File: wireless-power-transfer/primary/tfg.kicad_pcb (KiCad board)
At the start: 2 copper layers, 160 x 100 mm, 30 parts, among them J1 CONN_01X06, J2 Screw_Terminal_1x02, J3 BARREL_JACK, Q1 IRLB8721PBF, Q2 IRLB8721PBF, Q3 IRLB8721PBF, Q4 IRLB8721PBF, U1 PIC18F45K20-I/PT, U2 IR2110, U3 IR2110, U4 R-78E15, U5 R-78E3.3, U6 XBEE_Wi-Fi

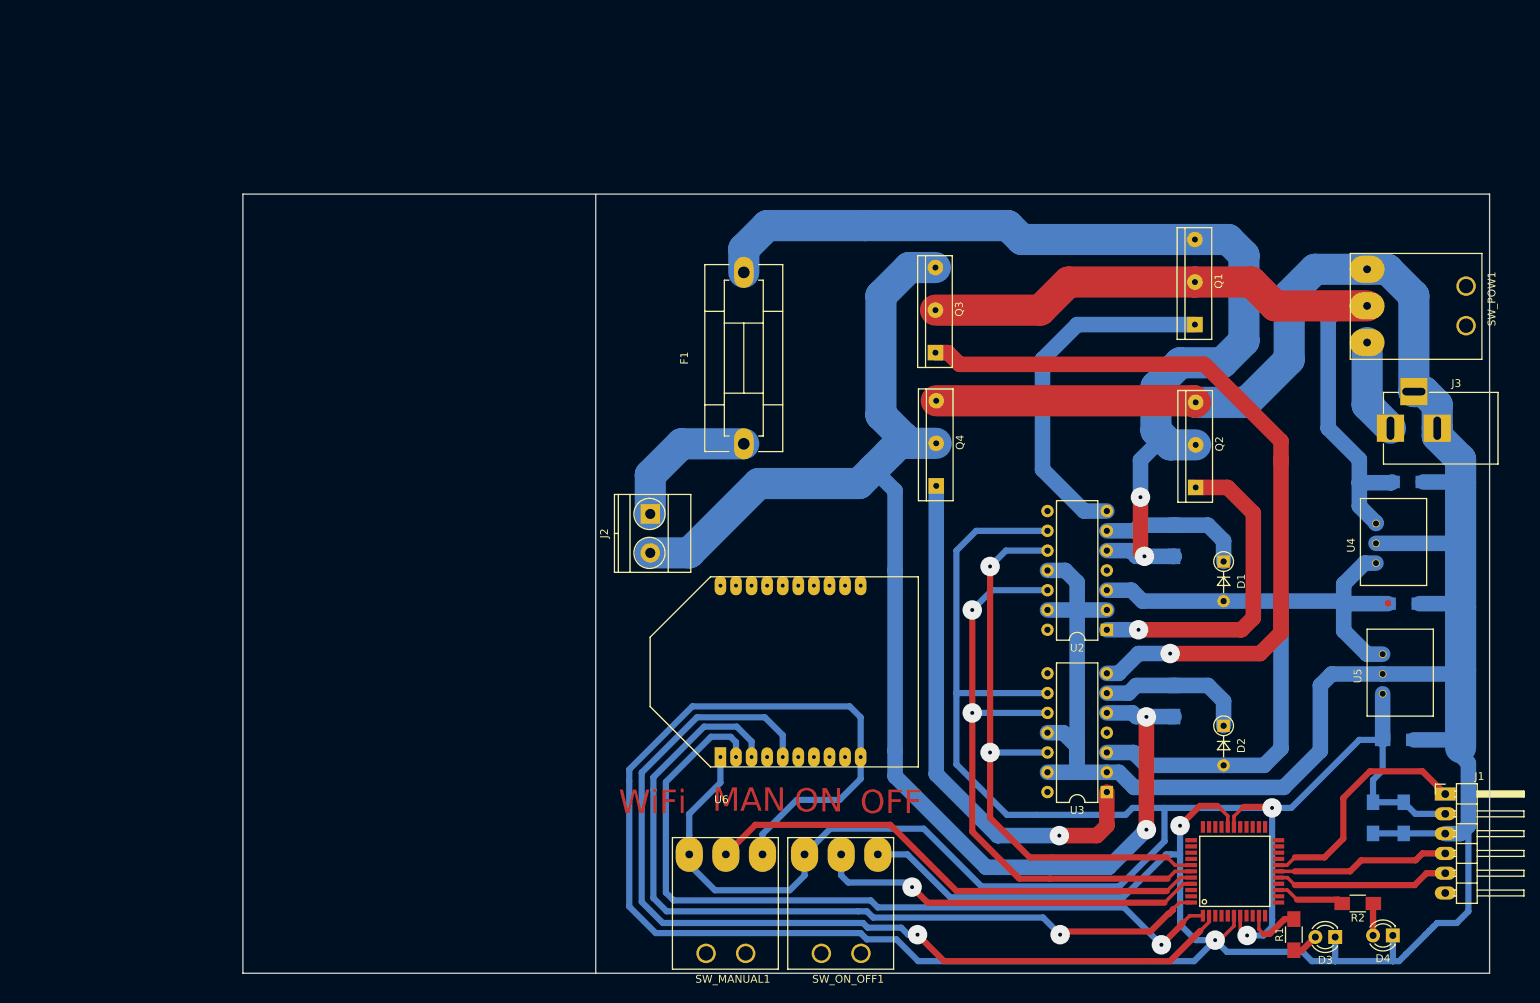
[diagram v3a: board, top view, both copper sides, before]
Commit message: Added pcb with tank and filter of the primary, some logos and other minor changes.
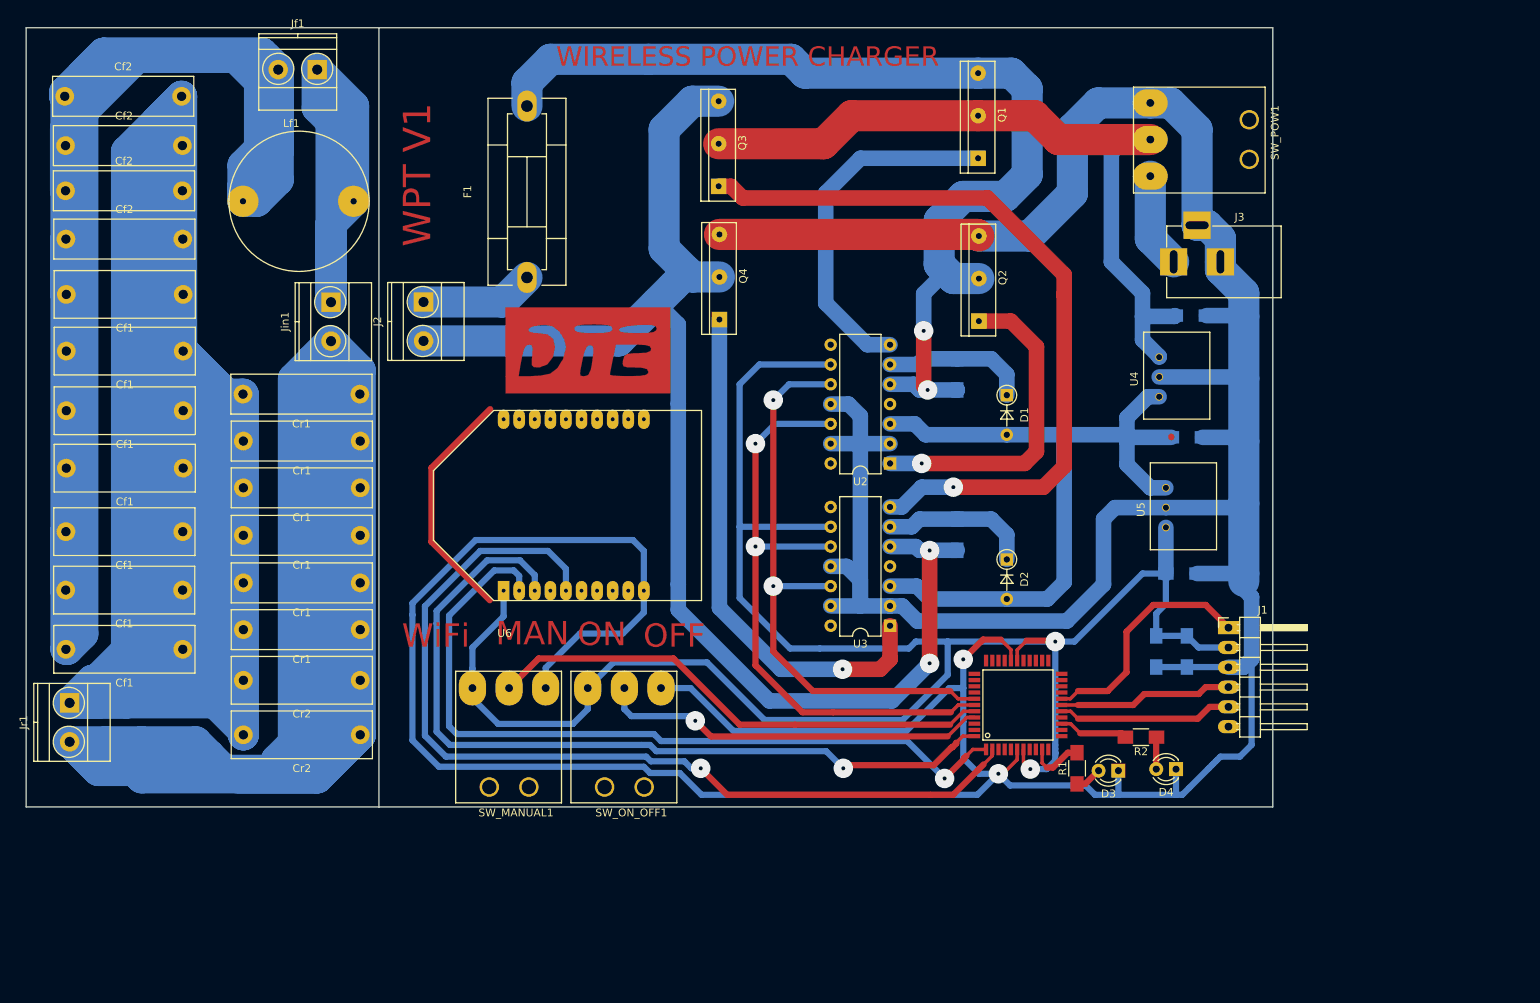
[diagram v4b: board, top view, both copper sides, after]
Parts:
- added Cf1: 10nF, Capacitors_THT:C_Rect_L18.0mm_W6.0mm_P15.00mm_FKS3_FKP3, F.Cu at (78.0, 59.8)
- added Cf1: C, Capacitors_THT:C_Rect_L18.0mm_W6.0mm_P15.00mm_FKS3_FKP3, F.Cu at (78.0, 67.1)
- added Cf1: C, Capacitors_THT:C_Rect_L18.0mm_W6.0mm_P15.00mm_FKS3_FKP3, F.Cu at (78.0, 74.8)
- added Cf1: C, Capacitors_THT:C_Rect_L18.0mm_W6.0mm_P15.00mm_FKS3_FKP3, F.Cu at (78.0, 82.1)
- added Cf1: C, Capacitors_THT:C_Rect_L18.0mm_W6.0mm_P15.00mm_FKS3_FKP3, F.Cu at (78.0, 90.3)
- added Cf1: C, Capacitors_THT:C_Rect_L18.0mm_W6.0mm_P15.00mm_FKS3_FKP3, F.Cu at (78.0, 97.8)
- added Cf1: C, Capacitors_THT:C_Rect_L18.0mm_W6.0mm_P15.00mm_FKS3_FKP3, F.Cu at (78.0, 105.4)
- added Cf2: 2.2nF, Capacitors_THT:C_Rect_L18.0mm_W5.0mm_P15.00mm_FKS3_FKP3, F.Cu at (62.9, 34.4)
- added Cf2: C, Capacitors_THT:C_Rect_L18.0mm_W5.0mm_P15.00mm_FKS3_FKP3, F.Cu at (63.0, 40.7)
- added Cf2: C, Capacitors_THT:C_Rect_L18.0mm_W5.0mm_P15.00mm_FKS3_FKP3, F.Cu at (63.0, 46.5)
- added Cf2: C, Capacitors_THT:C_Rect_L18.0mm_W5.0mm_P15.00mm_FKS3_FKP3, F.Cu at (63.0, 52.7)
- added Cr1: 100nF, Capacitors_THT:C_Rect_L18.0mm_W5.0mm_P15.00mm_FKS3_FKP3, F.Cu at (100.7, 72.6)
- added Cr1: 100nF, Capacitors_THT:C_Rect_L18.0mm_W5.0mm_P15.00mm_FKS3_FKP3, F.Cu at (100.8, 78.7)
- added Cr1: 100nF, Capacitors_THT:C_Rect_L18.0mm_W5.0mm_P15.00mm_FKS3_FKP3, F.Cu at (100.8, 84.7)
- added Cr1: 100nF, Capacitors_THT:C_Rect_L18.0mm_W5.0mm_P15.00mm_FKS3_FKP3, F.Cu at (100.8, 90.8)
- added Cr1: 100nF, Capacitors_THT:C_Rect_L18.0mm_W5.0mm_P15.00mm_FKS3_FKP3, F.Cu at (100.8, 96.8)
- added Cr1: 100nF, Capacitors_THT:C_Rect_L18.0mm_W5.0mm_P15.00mm_FKS3_FKP3, F.Cu at (100.8, 102.8)
- added Cr2: 10nF, Capacitors_THT:C_Rect_L18.0mm_W6.0mm_P15.00mm_FKS3_FKP3, F.Cu at (100.8, 116.3)
- added Cr2: 10nF, Capacitors_THT:C_Rect_L18.0mm_W6.0mm_P15.00mm_FKS3_FKP3, F.Cu at (100.8, 109.3)
- added G***: LOGO, componentesGIT:DTE, F.Cu at (130.0, 67.0)
- added Jf1: Screw_Terminal_1x02, Connectors_Terminal_Blocks:TerminalBlock_Pheonix_MKDS1.5-2pol, F.Cu at (95.2, 31.0)
- added Jin1: Screw_Terminal_1x02, Connectors_Terminal_Blocks:TerminalBlock_Pheonix_MKDS1.5-2pol, F.Cu at (97.0, 60.8)
- added Jr1: Screw_Terminal_1x02, Connectors_Terminal_Blocks:TerminalBlock_Pheonix_MKDS1.5-2pol, F.Cu at (63.5, 112.2)
- added Lf1: 47uH, componentesGIT:MuRata 1500 47u, F.Cu at (99.9, 47.9)
- moved J2 39.8 mm to (108.9, 60.8)
- moved C5 35.1 mm to (207.4, 62.5)
- moved D3 35.1 mm to (198.1, 121.0)
- moved D4 35.1 mm to (205.5, 120.8)
- moved Q1 35.1 mm to (180.1, 42.4)
- moved R2 35.1 mm to (201.0, 116.7)
- moved SW_ON_OFF1 35.1 mm to (130.0, 110.3)
- moved U2 35.1 mm to (168.8, 81.5)
- moved U3 35.1 mm to (168.8, 102.3)
- moved U6 35.1 mm to (119.2, 97.8)
- moved F1 35.1 mm to (122.2, 57.6)
- moved SW_MANUAL1 35.1 mm to (115.2, 110.3)
- moved C6 35.1 mm to (206.9, 78.2)
- moved Q4 35.1 mm to (146.9, 63.0)
- moved U1 35.1 mm to (189.1, 118.2)
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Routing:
- net Net-(Cf1-Pad1): track 0.00 -> 479.9 mm
- net Net-(Cr1-Pad1): track 0.00 -> 370.0 mm
- net Net-(Cf1-Pad2): track 0.00 -> 347.0 mm
- net Net-(Jf1-Pad1): track 0.00 -> 63.6 mm
- net (no net): track 0.09 -> 30.8 mm
- net Net-(F1-Pad1): track 18.7 -> 14.6 mm
- net Net-(Cboot2-Pad2): track 174.2 -> 173.1 mm
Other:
- board text added: "WIRELESS POWER CHARGER"
- board text added: "WPT V1"

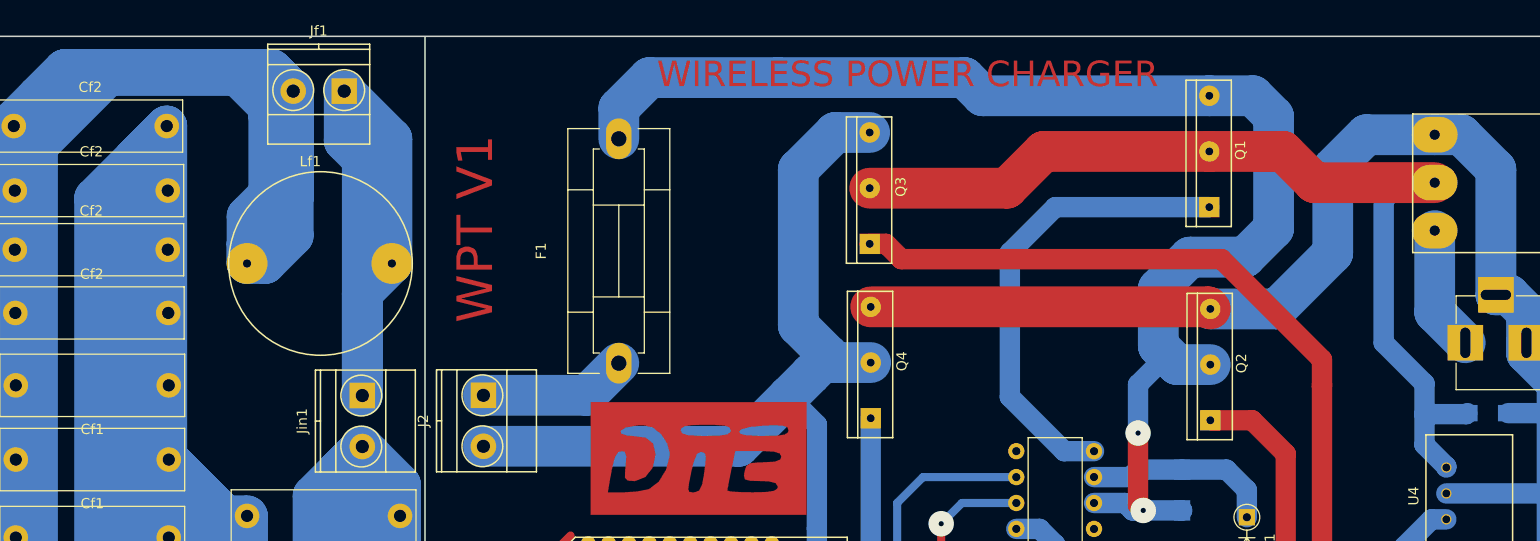
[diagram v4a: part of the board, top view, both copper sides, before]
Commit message: Modified secondary PCB for better fitting in the car.
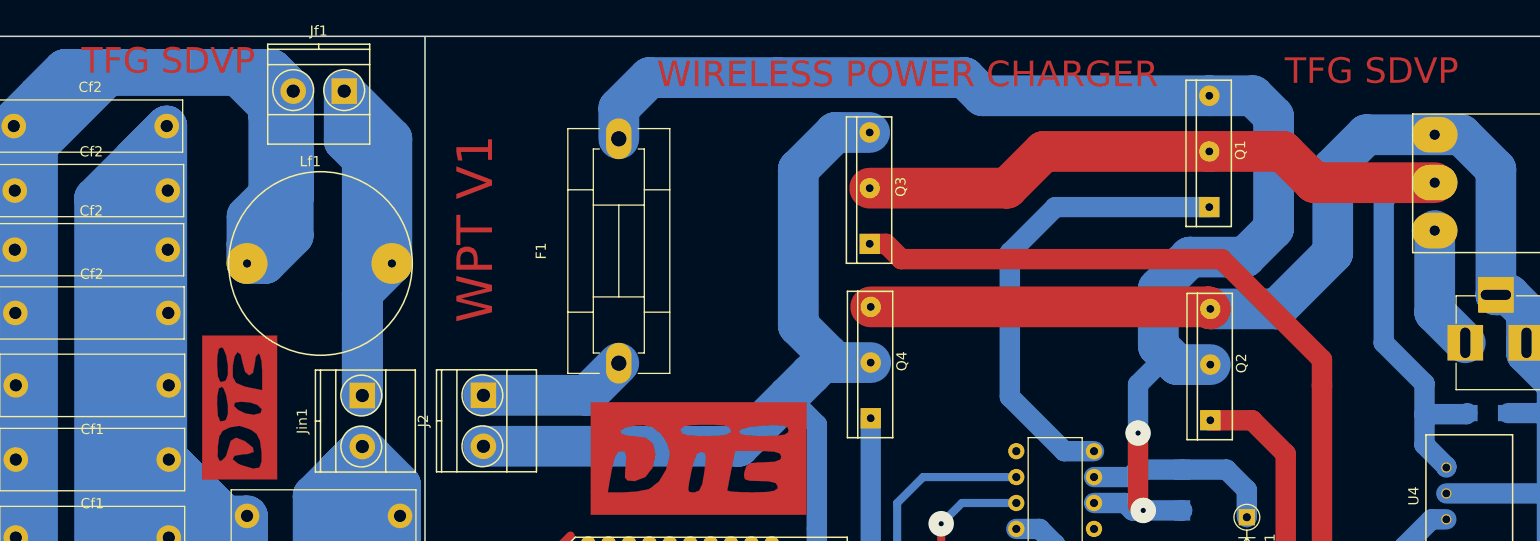
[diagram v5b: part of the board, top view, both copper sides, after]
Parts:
- added G***: LOGO, componentesGIT:DTE_Micro, F.Cu at (85.0, 62.0)
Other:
- board text added: "TFG SDVP"
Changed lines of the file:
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@@
     (area 56.3 23.8 223.280001 127.727)
     (thickness 1.6)
-    (drawings 19)
+    (drawings 21)
     (tracks 579)
     (zones 0)
-    (modules 54)
+    (modules 55)
     (nets 77)
   )
@@
   )
   (setup
-    (last_trace_width 4)
+    (last_trace_width 0.8)
     (user_trace_width 0.45)
     (user_trace_width 0.8)
@@
       (xy -8.897967 3.313043) (xy -10.583333 3.313043) (xy -10.583333 -5.521739) (xy 10.583333 -5.521739)
       (xy 10.583333 5.521739)) (layer F.Cu) (width 0.01))
+  )
+  (module componentesGIT:DTE_Micro (layer F.Cu)
+    (at 85 62 90)
+    (fp_text reference G*** (at 3 5 90) (layer F.SilkS) hide
+      (effects (font (thickness 0.3)))
+    )
+    (fp_text value LOGO (at -1 -5 90) (layer F.SilkS) hide
+      (effects (font (thickness 0.3)))
+    )
+    (fp_poly (pts (xy 7.055556 3.681159) (xy -7.055555 3.681159) (xy -7.055555 2.208696) (xy 1.707829 2.208696)
+      (xy 3.499748 2.208696) (xy 4.515097 2.143458) (xy 5.164544 1.976405) (xy 5.291667 1.84058)
+      (xy 4.985114 1.582113) (xy 4.2465 1.472492) (xy 4.233333 1.472464) (xy 3.401368 1.307936)
+      (xy 3.154326 0.935662) (xy 3.478527 0.537606) (xy 4.321528 0.29941) (xy 5.202345 0.095434)
+      (xy 5.42692 -0.203464) (xy 5.018786 -0.495004) (xy 4.09865 -0.669316) (xy 3.023344 -0.678138)
+      (xy 2.419037 -0.357361) (xy 2.073198 0.459307) (xy 1.949414 1.012319) (xy 1.707829 2.208696)
+      (xy -7.055555 2.208696) (xy -7.055555 1.328457) (xy -5.985372 1.328457) (xy -5.887546 1.933839)
+      (xy -5.271327 2.153272) (xy -4.332934 2.136836) (xy -3.229709 1.987754) (xy -2.574031 1.645596)
+      (xy -2.369213 1.358764) (xy -0.705555 1.358764) (xy -0.541721 2.051698) (xy -0.166878 2.171356)
+      (xy 0.243983 1.760742) (xy 0.483497 1.06654) (xy 0.57094 0.147434) (xy 0.474176 -0.460959)
+      (xy 0.473745 -0.46169) (xy 0.151341 -0.554444) (xy -0.240374 -0.14451) (xy -0.569845 0.56503)
+      (xy -0.705555 1.358764) (xy -2.369213 1.358764) (xy -2.139721 1.037378) (xy -1.798295 -0.020864)
+      (xy -1.958475 -0.98726) (xy -2.286304 -1.661404) (xy -2.667334 -1.894563) (xy -1.366925 -1.894563)
+      (xy -1.282289 -1.47517) (xy -1.159326 -1.332437) (xy -0.623942 -1.156524) (xy 0.252223 -1.162251)
+      (xy 1.177504 -1.311567) (xy 1.860235 -1.566425) (xy 2.030452 -1.748551) (xy 1.957835 -1.894563)
+      (xy 2.51363 -1.894563) (xy 2.598267 -1.47517) (xy 2.72123 -1.332437) (xy 3.256614 -1.156524)
+      (xy 4.132779 -1.162251) (xy 5.058059 -1.311567) (xy 5.740791 -1.566425) (xy 5.911008 -1.748551)
+      (xy 5.765432 -2.041259) (xy 5.043581 -2.185147) (xy 4.262732 -2.208696) (xy 3.058004 -2.133132)
+      (xy 2.51363 -1.894563) (xy 1.957835 -1.894563) (xy 1.884876 -2.041259) (xy 1.163026 -2.185147)
+      (xy 0.382176 -2.208696) (xy -0.822552 -2.133132) (xy -1.366925 -1.894563) (xy -2.667334 -1.894563)
+      (xy -2.832943 -1.995902) (xy -3.835668 -2.139707) (xy -4.81399 -2.154547) (xy -5.210979 -1.983469)
+      (xy -5.212598 -1.771591) (xy -4.781138 -1.353016) (xy -4.205701 -1.165206) (xy -3.255826 -0.880097)
+      (xy -2.956663 -0.353027) (xy -3.274237 0.480216) (xy -3.30708 0.533272) (xy -3.925002 1.300933)
+      (xy -4.356336 1.375278) (xy -4.569145 0.760432) (xy -4.586111 0.368116) (xy -4.724004 -0.496511)
+      (xy -5.06238 -0.684596) (xy -5.48829 -0.179191) (xy -5.653176 0.208022) (xy -5.985372 1.328457)
+      (xy -7.055555 1.328457) (xy -7.055555 -3.681159) (xy 7.055556 -3.681159) (xy 7.055556 3.681159)) (layer F.Cu) (width 0.01))
+  )
+  (gr_text "TFG SDVP" (at 78 28) (layer F.Cu)
+    (effects (font (size 2.5 2.5) (thickness 0.5)))
+  )
+  (gr_text "TFG SDVP" (at 196 29) (layer F.Cu)
+    (effects (font (size 2.5 2.5) (thickness 0.5)))
   )
   (gr_text "WIRELESS POWER CHARGER" (at 150.5 29.325) (layer F.Cu)
@@
   (segment (start 70.775 105.5) (end 70.9 105.375) (width 4) (layer B.Cu) (net 73))
   (segment (start 70.9 105.375) (end 78 105.375) (width 4) (layer B.Cu) (net 73))
-  (segment (start 63 52.725) (end 63 59.775) (width 4) (layer B.Cu) (net 74) (status C00000))
-  (segment (start 63 59.775) (end 63.05 59.825) (width 4) (layer B.Cu) (net 74) (status C00000))
-  (segment (start 62.95 40.725) (end 62.95 46.525) (width 4) (layer B.Cu) (net 74) (status C00000))
-  (segment (start 62.975 97.775) (end 62.975 90.3) (width 4) (layer B.Cu) (net 74) (status C00000))
-  (segment (start 62.975 90.3) (end 63 90.275) (width 4) (layer B.Cu) (net 74) (status C00000))
+  (segment (start 63 52.725) (end 63 59.775) (width 4) (layer B.Cu) (net 74))
+  (segment (start 63 59.775) (end 63.05 59.825) (width 4) (layer B.Cu) (net 74))
+  (segment (start 62.95 40.725) (end 62.95 46.525) (width 4) (layer B.Cu) (net 74))
+  (segment (start 62.975 97.775) (end 62.975 90.3) (width 4) (layer B.Cu) (net 74))
+  (segment (start 62.975 90.3) (end 63 90.275) (width 4) (layer B.Cu) (net 74))
   (segment (start 85.725 47.875) (end 85.725 43.25) (width 4) (layer B.Cu) (net 74))
   (segment (start 87.85 33.375) (end 90.25 30.975) (width 4) (layer B.Cu) (net 74))

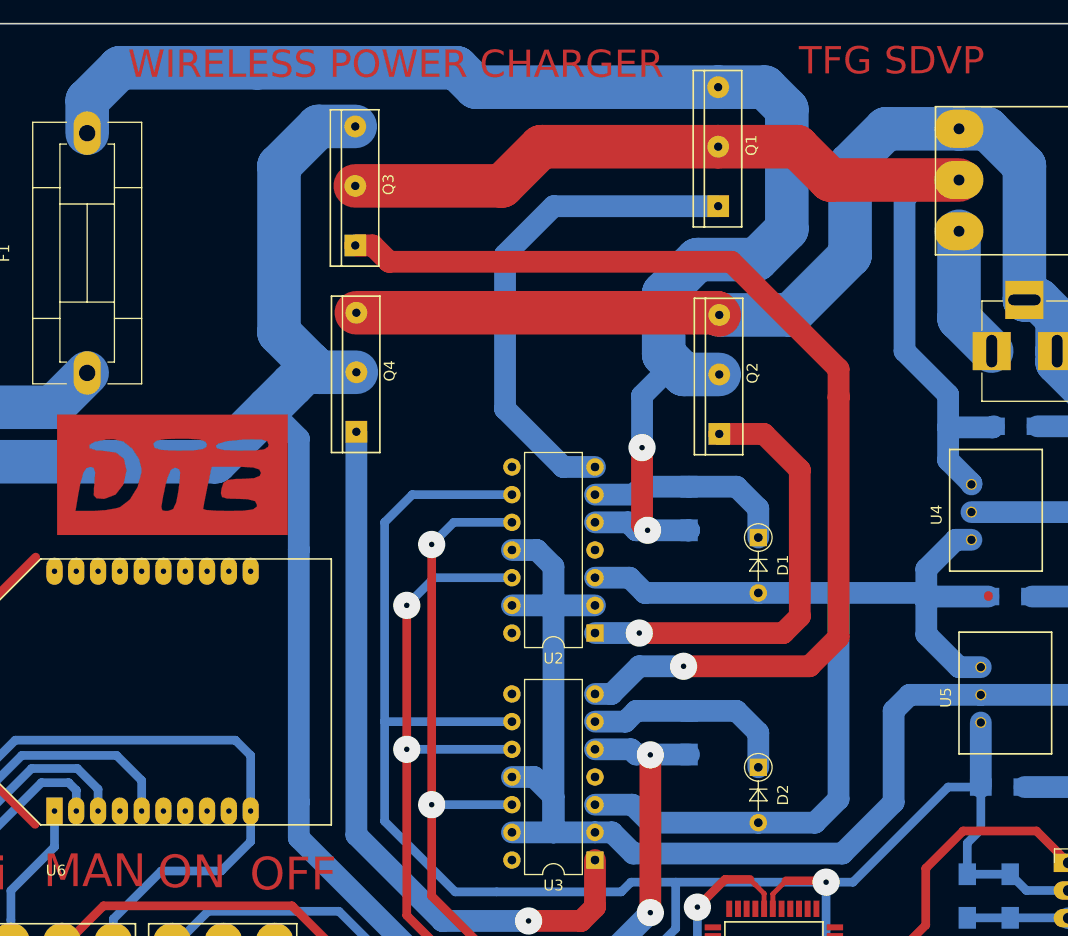
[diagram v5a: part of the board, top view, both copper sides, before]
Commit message: modified pad sizes and secondary PCB layout.
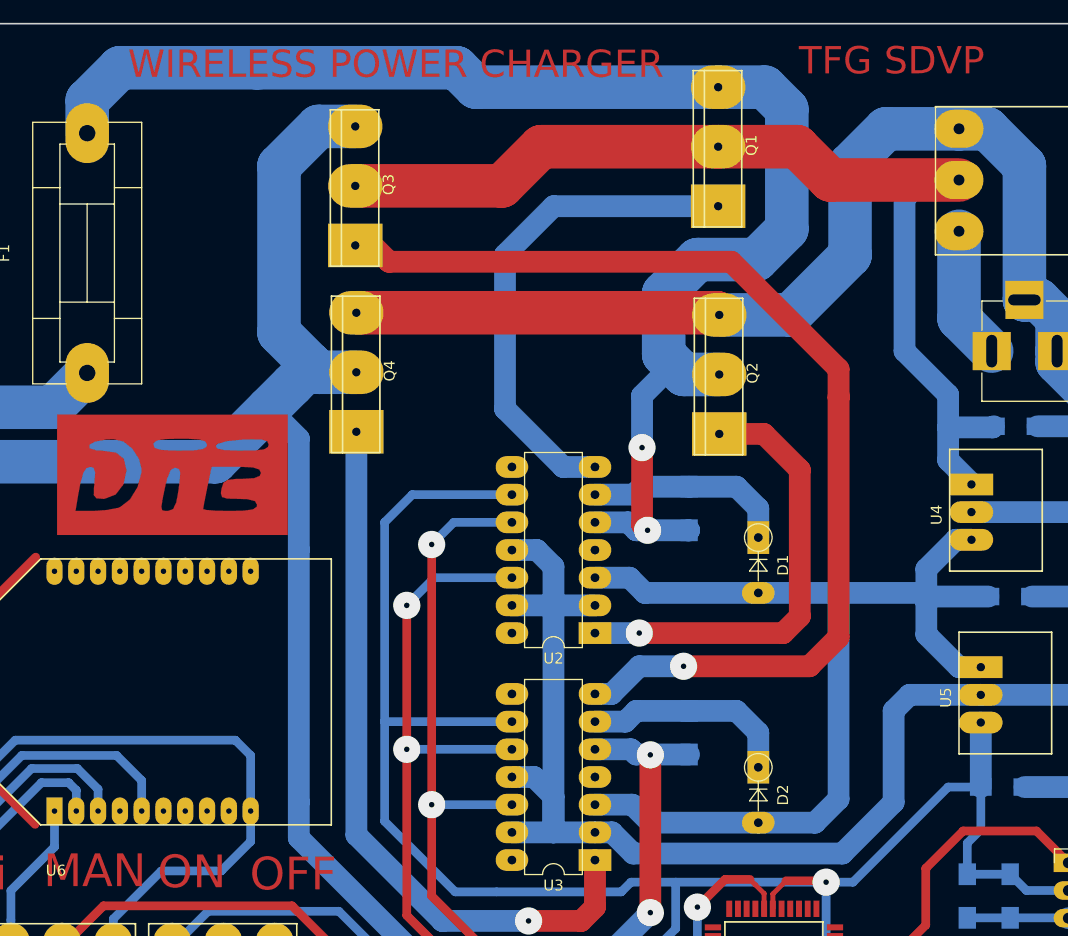
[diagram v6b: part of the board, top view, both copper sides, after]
